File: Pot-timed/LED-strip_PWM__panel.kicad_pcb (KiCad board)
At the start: 2 copper layers, 160 x 100 mm, 549 parts, among them IC1 ATTINY13A-MM, P1 CONN_2, P2 CONN_2, T1 AO3400, U1 MCP1804-SOT23-5

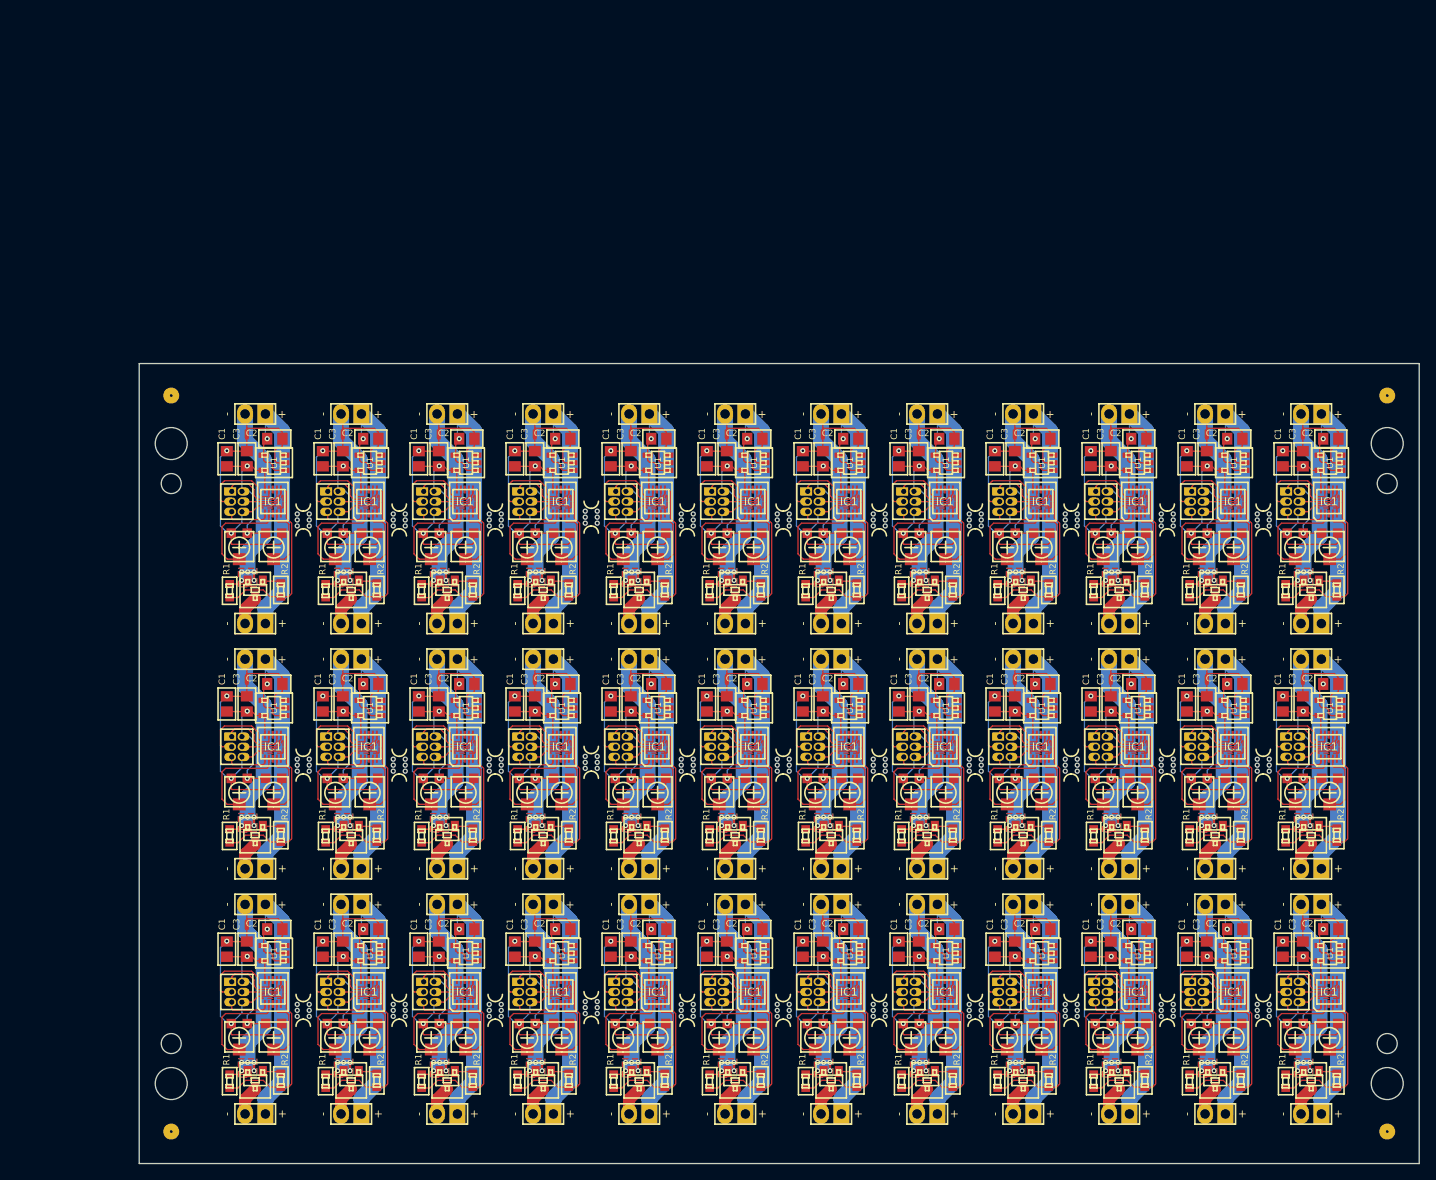
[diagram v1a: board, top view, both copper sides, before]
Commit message: Pot-timed: Reworking the panel.
KiCad really ought to know about the concept of 'linked clones' for boards.
Modify the 'parent' and all clones get updated automatically.
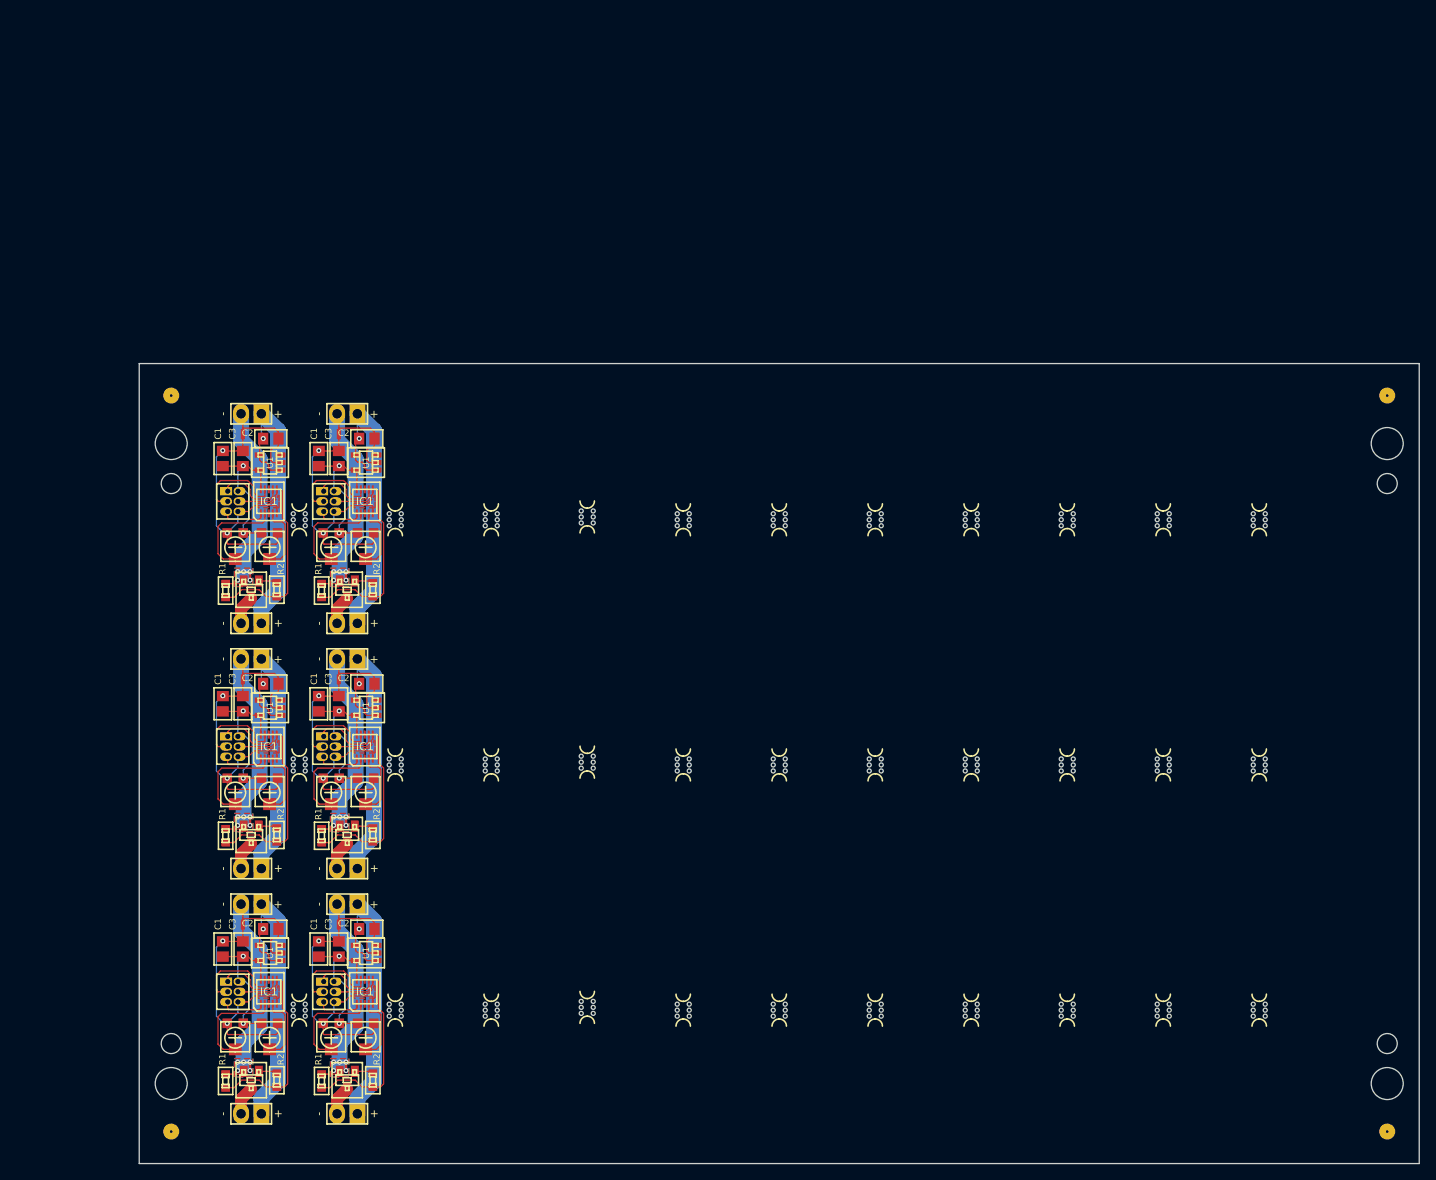
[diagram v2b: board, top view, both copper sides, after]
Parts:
- removed the C1 at (111.0, 93.9)
- removed the C1 at (218.9, 93.9)
- removed the C1 at (230.9, 93.9)
- removed the C1 at (242.9, 93.9)
- removed the C1 at (242.9, 124.5)
- removed the C1 at (230.9, 124.5)
- removed the C1 at (218.9, 124.5)
- removed the C1 at (182.9, 124.5)
- removed the C1 at (194.9, 124.5)
- removed the C1 at (206.9, 124.5)
- removed the C1 at (170.9, 124.5)
- removed the C1 at (146.9, 93.9)
- removed the C1 at (158.9, 124.5)
- removed the C1 at (123.0, 124.5)
- removed the C1 at (134.9, 124.5)
- removed the C1 at (146.9, 124.5)
- removed the C1 at (111.0, 124.5)
- removed the C1 at (111.0, 155.2)
- removed the C1 at (146.9, 155.2)
- removed the C1 at (134.9, 155.2)
- removed the C1 at (123.0, 155.2)
- removed the C1 at (158.9, 155.2)
- removed the C1 at (134.9, 93.9)
- removed the C1 at (170.9, 155.2)
- removed the C1 at (206.9, 155.2)
- removed the C1 at (194.9, 155.2)
- removed the C1 at (182.9, 155.2)
- removed the C1 at (218.9, 155.2)
- removed the C1 at (230.9, 155.2)
- removed the C1 at (242.9, 155.2)
- removed the C1 at (123.0, 93.9)
- removed the C1 at (158.9, 93.9)
- removed the C1 at (170.9, 93.9)
- removed the C1 at (206.9, 93.9)
- removed the C1 at (194.9, 93.9)
- removed the C1 at (182.9, 93.9)
- removed the C2 at (117.0, 91.4)
- removed the C2 at (224.9, 91.4)
- removed the C2 at (236.9, 91.4)
- removed the C2 at (248.9, 91.4)
- removed the C2 at (248.9, 122.0)
- removed the C2 at (236.9, 122.0)
- removed the C2 at (224.9, 122.0)
- removed the C2 at (188.9, 122.0)
- removed the C2 at (200.9, 122.0)
- removed the C2 at (212.9, 122.0)
- removed the C2 at (176.9, 122.0)
- removed the C2 at (152.9, 91.4)
- removed the C2 at (164.9, 122.0)
- removed the C2 at (128.9, 122.0)
- removed the C2 at (140.9, 122.0)
- removed the C2 at (152.9, 122.0)
- removed the C2 at (117.0, 122.0)
- removed the C2 at (117.0, 152.7)
- removed the C2 at (152.9, 152.7)
- removed the C2 at (140.9, 152.7)
- removed the C2 at (128.9, 152.7)
- removed the C2 at (164.9, 152.7)
- removed the C2 at (140.9, 91.4)
- removed the C2 at (176.9, 152.7)
- removed the C2 at (212.9, 152.7)
- removed the C2 at (200.9, 152.7)
- removed the C2 at (188.9, 152.7)
- removed the C2 at (224.9, 152.7)
- removed the C2 at (236.9, 152.7)
- removed the C2 at (248.9, 152.7)
- removed the C2 at (128.9, 91.4)
- removed the C2 at (164.9, 91.4)
- removed the C2 at (176.9, 91.4)
- removed the C2 at (212.9, 91.4)
- removed the C2 at (200.9, 91.4)
- removed the C2 at (188.9, 91.4)
- removed the C3 at (113.5, 93.9)
- removed the C3 at (221.4, 93.9)
- removed the C3 at (233.4, 93.9)
- removed the C3 at (245.4, 93.9)
- removed the C3 at (245.4, 124.5)
- removed the C3 at (233.4, 124.5)
- removed the C3 at (221.4, 124.5)
- removed the C3 at (185.4, 124.5)
- removed the C3 at (197.4, 124.5)
- removed the C3 at (209.4, 124.5)
- removed the C3 at (173.4, 124.5)
- removed the C3 at (149.4, 93.9)
- removed the C3 at (161.4, 124.5)
- removed the C3 at (125.5, 124.5)
- removed the C3 at (137.4, 124.5)
- removed the C3 at (149.4, 124.5)
- removed the C3 at (113.5, 124.5)
- removed the C3 at (113.5, 155.2)
- removed the C3 at (149.4, 155.2)
- removed the C3 at (137.4, 155.2)
- removed the C3 at (125.5, 155.2)
- removed the C3 at (161.4, 155.2)
- removed the C3 at (137.4, 93.9)
- removed the C3 at (173.4, 155.2)
- removed the C3 at (209.4, 155.2)
- removed the C3 at (197.4, 155.2)
- removed the C3 at (185.4, 155.2)
- removed the C3 at (221.4, 155.2)
- removed the C3 at (233.4, 155.2)
- removed the C3 at (245.4, 155.2)
- removed the C3 at (125.5, 93.9)
- removed the C3 at (161.4, 93.9)
- removed the C3 at (173.4, 93.9)
- removed the C3 at (209.4, 93.9)
- removed the C3 at (197.4, 93.9)
- removed the C3 at (185.4, 93.9)
- removed the IC1 at (116.7, 99.2)
- removed the IC1 at (224.7, 99.2)
- removed the IC1 at (236.7, 99.2)
- removed the IC1 at (248.7, 99.2)
- removed the IC1 at (248.7, 129.9)
- removed the IC1 at (236.7, 129.9)
- removed the IC1 at (224.7, 129.9)
- removed the IC1 at (188.7, 129.9)
- removed the IC1 at (200.7, 129.9)
- removed the IC1 at (212.7, 129.9)
- removed the IC1 at (176.7, 129.9)
- removed the IC1 at (152.7, 99.2)
- removed the IC1 at (164.7, 129.9)
- removed the IC1 at (128.7, 129.9)
- removed the IC1 at (140.7, 129.9)
- removed the IC1 at (152.7, 129.9)
- removed the IC1 at (116.7, 129.9)
- removed the IC1 at (116.7, 160.6)
- removed the IC1 at (152.7, 160.6)
- removed the IC1 at (140.7, 160.6)
- removed the IC1 at (128.7, 160.6)
- removed the IC1 at (164.7, 160.6)
- removed the IC1 at (140.7, 99.2)
- removed the IC1 at (176.7, 160.6)
- removed the IC1 at (212.7, 160.6)
- removed the IC1 at (200.7, 160.6)
- removed the IC1 at (188.7, 160.6)
- removed the IC1 at (224.7, 160.6)
- removed the IC1 at (236.7, 160.6)
- removed the IC1 at (248.7, 160.6)
- removed the IC1 at (128.7, 99.2)
- removed the IC1 at (164.7, 99.2)
- removed the IC1 at (176.7, 99.2)
- removed the IC1 at (212.7, 99.2)
- removed the IC1 at (200.7, 99.2)
- removed the IC1 at (188.7, 99.2)
- removed the JP1 at (112.2, 99.2)
- removed the JP1 at (220.2, 99.2)
- removed the JP1 at (232.2, 99.2)
- removed the JP1 at (244.2, 99.2)
- removed the JP1 at (244.2, 129.9)
- removed the JP1 at (232.2, 129.9)
- removed the JP1 at (220.2, 129.9)
- removed the JP1 at (184.2, 129.9)
- removed the JP1 at (196.2, 129.9)
- removed the JP1 at (208.2, 129.9)
- removed the JP1 at (172.2, 129.9)
- removed the JP1 at (148.2, 99.2)
- removed the JP1 at (160.2, 129.9)
- removed the JP1 at (124.2, 129.9)
- removed the JP1 at (136.2, 129.9)
- removed the JP1 at (148.2, 129.9)
- removed the JP1 at (112.2, 129.9)
- removed the JP1 at (112.2, 160.6)
- removed the JP1 at (148.2, 160.6)
- removed the JP1 at (136.2, 160.6)
- removed the JP1 at (124.2, 160.6)
- removed the JP1 at (160.2, 160.6)
- removed the JP1 at (136.2, 99.2)
- removed the JP1 at (172.2, 160.6)
- removed the JP1 at (208.2, 160.6)
- removed the JP1 at (196.2, 160.6)
- removed the JP1 at (184.2, 160.6)
- removed the JP1 at (220.2, 160.6)
- removed the JP1 at (232.2, 160.6)
- removed the JP1 at (244.2, 160.6)
- removed the JP1 at (124.2, 99.2)
- removed the JP1 at (160.2, 99.2)
- removed the JP1 at (172.2, 99.2)
- removed the JP1 at (208.2, 99.2)
- removed the JP1 at (196.2, 99.2)
- removed the JP1 at (184.2, 99.2)
- removed the NJ1 at (113.5, 90.8)
- removed the NJ1 at (221.4, 90.8)
- removed the NJ1 at (233.4, 90.8)
- removed the NJ1 at (245.4, 90.8)
- removed the NJ1 at (245.4, 121.5)
- removed the NJ1 at (233.4, 121.5)
- removed the NJ1 at (221.4, 121.5)
- removed the NJ1 at (185.4, 121.5)
- removed the NJ1 at (197.4, 121.5)
- removed the NJ1 at (209.4, 121.5)
- removed the NJ1 at (173.4, 121.5)
- removed the NJ1 at (149.4, 90.8)
- removed the NJ1 at (161.4, 121.5)
- removed the NJ1 at (125.5, 121.5)
- removed the NJ1 at (137.4, 121.5)
- removed the NJ1 at (149.4, 121.5)
- removed the NJ1 at (113.5, 121.5)
- removed the NJ1 at (113.5, 152.2)
- removed the NJ1 at (149.4, 152.2)
- removed the NJ1 at (137.4, 152.2)
- removed the NJ1 at (125.5, 152.2)
- removed the NJ1 at (161.4, 152.2)
- removed the NJ1 at (137.4, 90.8)
- removed the NJ1 at (173.4, 152.2)
- removed the NJ1 at (209.4, 152.2)
- removed the NJ1 at (197.4, 152.2)
- removed the NJ1 at (185.4, 152.2)
- removed the NJ1 at (221.4, 152.2)
- removed the NJ1 at (233.4, 152.2)
- removed the NJ1 at (245.4, 152.2)
- removed the NJ1 at (125.5, 90.8)
- removed the NJ1 at (161.4, 90.8)
- removed the NJ1 at (173.4, 90.8)
- removed the NJ1 at (209.4, 90.8)
- removed the NJ1 at (197.4, 90.8)
- removed the NJ1 at (185.4, 90.8)
- removed the P1 at (114.5, 88.3)
- removed the P1 at (222.5, 88.3)
- removed the P1 at (234.5, 88.3)
- removed the P1 at (246.5, 88.3)
- removed the P1 at (246.5, 119.0)
- removed the P1 at (234.5, 119.0)
- removed the P1 at (222.5, 119.0)
- removed the P1 at (186.5, 119.0)
- removed the P1 at (198.5, 119.0)
- removed the P1 at (210.5, 119.0)
- removed the P1 at (174.5, 119.0)
- removed the P1 at (150.5, 88.3)
- removed the P1 at (162.5, 119.0)
- removed the P1 at (126.5, 119.0)
- removed the P1 at (138.5, 119.0)
- removed the P1 at (150.5, 119.0)
- removed the P1 at (114.5, 119.0)
- removed the P1 at (114.5, 149.6)
- removed the P1 at (150.5, 149.6)
- removed the P1 at (138.5, 149.6)
- removed the P1 at (126.5, 149.6)
- removed the P1 at (162.5, 149.6)
- removed the P1 at (138.5, 88.3)
- removed the P1 at (174.5, 149.6)
- removed the P1 at (210.5, 149.6)
- removed the P1 at (198.5, 149.6)
- removed the P1 at (186.5, 149.6)
- removed the P1 at (222.5, 149.6)
- removed the P1 at (234.5, 149.6)
- removed the P1 at (246.5, 149.6)
- removed the P1 at (126.5, 88.3)
- removed the P1 at (162.5, 88.3)
- removed the P1 at (174.5, 88.3)
- removed the P1 at (210.5, 88.3)
- removed the P1 at (198.5, 88.3)
- removed the P1 at (186.5, 88.3)
- removed the P2 at (114.5, 114.5)
- removed the P2 at (222.5, 114.5)
- removed the P2 at (234.5, 114.5)
- removed the P2 at (246.5, 114.5)
- removed the P2 at (246.5, 145.2)
- removed the P2 at (234.5, 145.2)
- removed the P2 at (222.5, 145.2)
- removed the P2 at (186.5, 145.2)
- removed the P2 at (198.5, 145.2)
- removed the P2 at (210.5, 145.2)
- removed the P2 at (174.5, 145.2)
- removed the P2 at (150.5, 114.5)
- removed the P2 at (162.5, 145.2)
- removed the P2 at (126.5, 145.2)
- removed the P2 at (138.5, 145.2)
- removed the P2 at (150.5, 145.2)
- removed the P2 at (114.5, 145.2)
- removed the P2 at (114.5, 175.8)
- removed the P2 at (150.5, 175.8)
- removed the P2 at (138.5, 175.8)
- removed the P2 at (126.5, 175.8)
- removed the P2 at (162.5, 175.8)
- removed the P2 at (138.5, 114.5)
- removed the P2 at (174.5, 175.8)
- removed the P2 at (210.5, 175.8)
- removed the P2 at (198.5, 175.8)
- removed the P2 at (186.5, 175.8)
- removed the P2 at (222.5, 175.8)
- removed the P2 at (234.5, 175.8)
- removed the P2 at (246.5, 175.8)
- removed the P2 at (126.5, 114.5)
- removed the P2 at (162.5, 114.5)
- removed the P2 at (174.5, 114.5)
- removed the P2 at (210.5, 114.5)
- removed the P2 at (198.5, 114.5)
- removed the P2 at (186.5, 114.5)
- removed the R1 at (111.3, 110.4)
- removed the R1 at (219.3, 110.4)
- removed the R1 at (231.3, 110.4)
- removed the R1 at (243.3, 110.4)
- removed the R1 at (243.3, 141.1)
- removed the R1 at (231.3, 141.1)
- removed the R1 at (219.3, 141.1)
- removed the R1 at (183.3, 141.1)
- removed the R1 at (195.3, 141.1)
- removed the R1 at (207.3, 141.1)
- removed the R1 at (171.3, 141.1)
- removed the R1 at (147.3, 110.4)
- removed the R1 at (159.3, 141.1)
- removed the R1 at (123.3, 141.1)
- removed the R1 at (135.3, 141.1)
- removed the R1 at (147.3, 141.1)
- removed the R1 at (111.3, 141.1)
- removed the R1 at (111.3, 171.7)
- removed the R1 at (147.3, 171.7)
- removed the R1 at (135.3, 171.7)
- removed the R1 at (123.3, 171.7)
- removed the R1 at (159.3, 171.7)
- removed the R1 at (135.3, 110.4)
- removed the R1 at (171.3, 171.7)
- removed the R1 at (207.3, 171.7)
- removed the R1 at (195.3, 171.7)
- removed the R1 at (183.3, 171.7)
- removed the R1 at (219.3, 171.7)
- removed the R1 at (231.3, 171.7)
- removed the R1 at (243.3, 171.7)
- removed the R1 at (123.3, 110.4)
- removed the R1 at (159.3, 110.4)
- removed the R1 at (171.3, 110.4)
- removed the R1 at (207.3, 110.4)
- removed the R1 at (195.3, 110.4)
- removed the R1 at (183.3, 110.4)
- removed the R2 at (117.7, 110.3)
- removed the R2 at (225.7, 110.3)
- removed the R2 at (237.7, 110.3)
- removed the R2 at (249.7, 110.3)
- removed the R2 at (249.7, 140.9)
- removed the R2 at (237.7, 140.9)
- removed the R2 at (225.7, 140.9)
- removed the R2 at (189.7, 140.9)
- removed the R2 at (201.7, 140.9)
- removed the R2 at (213.7, 140.9)
- removed the R2 at (177.7, 140.9)
- removed the R2 at (153.7, 110.3)
- removed the R2 at (165.7, 140.9)
- removed the R2 at (129.7, 140.9)
- removed the R2 at (141.7, 140.9)
- removed the R2 at (153.7, 140.9)
- removed the R2 at (117.7, 140.9)
- removed the R2 at (117.7, 171.6)
- removed the R2 at (153.7, 171.6)
- removed the R2 at (141.7, 171.6)
- removed the R2 at (129.7, 171.6)
- removed the R2 at (165.7, 171.6)
- removed the R2 at (141.7, 110.3)
- removed the R2 at (177.7, 171.6)
- removed the R2 at (213.7, 171.6)
- removed the R2 at (201.7, 171.6)
- removed the R2 at (189.7, 171.6)
- removed the R2 at (225.7, 171.6)
- removed the R2 at (237.7, 171.6)
- removed the R2 at (249.7, 171.6)
- removed the R2 at (129.7, 110.3)
- removed the R2 at (165.7, 110.3)
- removed the R2 at (177.7, 110.3)
- removed the R2 at (213.7, 110.3)
- removed the R2 at (201.7, 110.3)
- removed the R2 at (189.7, 110.3)
- removed the RV1 at (112.5, 105.0)
- removed the RV1 at (220.5, 105.0)
- removed the RV1 at (232.5, 105.0)
- removed the RV1 at (244.5, 105.0)
- removed the RV1 at (244.5, 135.7)
- removed the RV1 at (232.5, 135.7)
- removed the RV1 at (220.5, 135.7)
- removed the RV1 at (184.5, 135.7)
- removed the RV1 at (196.5, 135.7)
- removed the RV1 at (208.5, 135.7)
- removed the RV1 at (172.5, 135.7)
- removed the RV1 at (148.5, 105.0)
- removed the RV1 at (160.5, 135.7)
- removed the RV1 at (124.5, 135.7)
- removed the RV1 at (136.5, 135.7)
- removed the RV1 at (148.5, 135.7)
- removed the RV1 at (112.5, 135.7)
- removed the RV1 at (112.5, 166.3)
- removed the RV1 at (148.5, 166.3)
- removed the RV1 at (136.5, 166.3)
- removed the RV1 at (124.5, 166.3)
- removed the RV1 at (160.5, 166.3)
- removed the RV1 at (136.5, 105.0)
- removed the RV1 at (172.5, 166.3)
- removed the RV1 at (208.5, 166.3)
- removed the RV1 at (196.5, 166.3)
- removed the RV1 at (184.5, 166.3)
- removed the RV1 at (220.5, 166.3)
- removed the RV1 at (232.5, 166.3)
- removed the RV1 at (244.5, 166.3)
- removed the RV1 at (124.5, 105.0)
- removed the RV1 at (160.5, 105.0)
- removed the RV1 at (172.5, 105.0)
- removed the RV1 at (208.5, 105.0)
- removed the RV1 at (196.5, 105.0)
- removed the RV1 at (184.5, 105.0)
- removed the RV2 at (116.8, 105.0)
- removed the RV2 at (224.8, 105.0)
- removed the RV2 at (236.8, 105.0)
- removed the RV2 at (248.8, 105.0)
- removed the RV2 at (248.8, 135.7)
- removed the RV2 at (236.8, 135.7)
- removed the RV2 at (224.8, 135.7)
- removed the RV2 at (188.8, 135.7)
- removed the RV2 at (200.8, 135.7)
- removed the RV2 at (212.8, 135.7)
- removed the RV2 at (176.8, 135.7)
- removed the RV2 at (152.8, 105.0)
- removed the RV2 at (164.8, 135.7)
- removed the RV2 at (128.8, 135.7)
- removed the RV2 at (140.8, 135.7)
- removed the RV2 at (152.8, 135.7)
- removed the RV2 at (116.8, 135.7)
- removed the RV2 at (116.8, 166.3)
- removed the RV2 at (152.8, 166.3)
- removed the RV2 at (140.8, 166.3)
- removed the RV2 at (128.8, 166.3)
- removed the RV2 at (164.8, 166.3)
- removed the RV2 at (140.8, 105.0)
- removed the RV2 at (176.8, 166.3)
- removed the RV2 at (212.8, 166.3)
- removed the RV2 at (200.8, 166.3)
- removed the RV2 at (188.8, 166.3)
- removed the RV2 at (224.8, 166.3)
- removed the RV2 at (236.8, 166.3)
- removed the RV2 at (248.8, 166.3)
- removed the RV2 at (128.8, 105.0)
- removed the RV2 at (164.8, 105.0)
- removed the RV2 at (176.8, 105.0)
- removed the RV2 at (212.8, 105.0)
- removed the RV2 at (200.8, 105.0)
- removed the RV2 at (188.8, 105.0)
- removed the T1 at (114.5, 110.3)
- removed the T1 at (222.5, 110.3)
- removed the T1 at (234.5, 110.3)
- removed the T1 at (246.5, 110.3)
- removed the T1 at (246.5, 140.9)
- removed the T1 at (234.5, 140.9)
- removed the T1 at (222.5, 140.9)
- removed the T1 at (186.5, 140.9)
- removed the T1 at (198.5, 140.9)
- removed the T1 at (210.5, 140.9)
- removed the T1 at (174.5, 140.9)
- removed the T1 at (150.5, 110.3)
- removed the T1 at (162.5, 140.9)
- removed the T1 at (126.5, 140.9)
- removed the T1 at (138.5, 140.9)
- removed the T1 at (150.5, 140.9)
- removed the T1 at (114.5, 140.9)
- removed the T1 at (114.5, 171.6)
- removed the T1 at (150.5, 171.6)
- removed the T1 at (138.5, 171.6)
- removed the T1 at (126.5, 171.6)
- removed the T1 at (162.5, 171.6)
- removed the T1 at (138.5, 110.3)
- removed the T1 at (174.5, 171.6)
- removed the T1 at (210.5, 171.6)
- removed the T1 at (198.5, 171.6)
- removed the T1 at (186.5, 171.6)
- removed the T1 at (222.5, 171.6)
- removed the T1 at (234.5, 171.6)
- removed the T1 at (246.5, 171.6)
- removed the T1 at (126.5, 110.3)
- removed the T1 at (162.5, 110.3)
- removed the T1 at (174.5, 110.3)
- removed the T1 at (210.5, 110.3)
- removed the T1 at (198.5, 110.3)
- removed the T1 at (186.5, 110.3)
- removed the U1 at (116.8, 94.4)
- removed the U1 at (224.8, 94.4)
- removed the U1 at (236.8, 94.4)
- removed the U1 at (248.8, 94.4)
- removed the U1 at (248.8, 125.0)
- removed the U1 at (236.8, 125.0)
- removed the U1 at (224.8, 125.0)
- removed the U1 at (188.8, 125.0)
- removed the U1 at (200.8, 125.0)
- removed the U1 at (212.8, 125.0)
- removed the U1 at (176.8, 125.0)
- removed the U1 at (152.8, 94.4)
- removed the U1 at (164.8, 125.0)
- removed the U1 at (128.8, 125.0)
- removed the U1 at (140.8, 125.0)
- removed the U1 at (152.8, 125.0)
- removed the U1 at (116.8, 125.0)
- removed the U1 at (116.8, 155.7)
- removed the U1 at (152.8, 155.7)
- removed the U1 at (140.8, 155.7)
- removed the U1 at (128.8, 155.7)
- removed the U1 at (164.8, 155.7)
- removed the U1 at (140.8, 94.4)
- removed the U1 at (176.8, 155.7)
- removed the U1 at (212.8, 155.7)
- removed the U1 at (200.8, 155.7)
- removed the U1 at (188.8, 155.7)
- removed the U1 at (224.8, 155.7)
- removed the U1 at (236.8, 155.7)
- removed the U1 at (248.8, 155.7)
- removed the U1 at (128.8, 94.4)
- removed the U1 at (164.8, 94.4)
- removed the U1 at (176.8, 94.4)
- removed the U1 at (212.8, 94.4)
- removed the U1 at (200.8, 94.4)
- removed the U1 at (188.8, 94.4)
- added C1: 100nF, MADW__C0805, F.Cu at (122.5, 93.9)
- added C1: 100nF, MADW__C0805, F.Cu at (122.5, 124.5)
- added C1: 100nF, MADW__C0805, F.Cu at (122.5, 155.2)
- added C1: 100nF, MADW__C0805, F.Cu at (110.5, 155.2)
- added C1: 100nF, MADW__C0805, F.Cu at (110.5, 124.5)
- added C1: 100nF, MADW__C0805, F.Cu at (110.5, 93.9)
- added C2: 100nF, MADW__C0805, F.Cu at (128.4, 91.4)
- added C2: 100nF, MADW__C0805, F.Cu at (128.4, 122.0)
- added C2: 100nF, MADW__C0805, F.Cu at (128.4, 152.7)
- added C2: 100nF, MADW__C0805, F.Cu at (116.5, 152.7)
- added C2: 100nF, MADW__C0805, F.Cu at (116.5, 122.0)
- added C2: 100nF, MADW__C0805, F.Cu at (116.5, 91.4)
- added C3: 4.7µF, MADW__C0805, F.Cu at (125.0, 93.9)
- added C3: 4.7µF, MADW__C0805, F.Cu at (125.0, 124.5)
- added C3: 4.7µF, MADW__C0805, F.Cu at (125.0, 155.2)
- added C3: 4.7µF, MADW__C0805, F.Cu at (113.0, 155.2)
- added C3: 4.7µF, MADW__C0805, F.Cu at (113.0, 124.5)
- added C3: 4.7µF, MADW__C0805, F.Cu at (113.0, 93.9)
- added IC1: ATTINY13A-MM, MADW__MLF10, F.Cu at (128.2, 99.2)
- added IC1: ATTINY13A-MM, MADW__MLF10, F.Cu at (128.2, 129.9)
- added IC1: ATTINY13A-MM, MADW__MLF10, F.Cu at (128.2, 160.5)
- added IC1: ATTINY13A-MM, MADW__MLF10, F.Cu at (116.2, 160.5)
- added IC1: ATTINY13A-MM, MADW__MLF10, F.Cu at (116.2, 129.9)
- added IC1: ATTINY13A-MM, MADW__MLF10, F.Cu at (116.2, 99.2)
- added JP1: ISP, MADW__PIN_ARRAY_3x2_1.27mm, F.Cu at (123.7, 99.2)
- added JP1: ISP, MADW__PIN_ARRAY_3x2_1.27mm, F.Cu at (123.7, 129.9)
- added JP1: ISP, MADW__PIN_ARRAY_3x2_1.27mm, F.Cu at (123.7, 160.5)
- added JP1: ISP, MADW__PIN_ARRAY_3x2_1.27mm, F.Cu at (111.7, 160.5)
- added JP1: ISP, MADW__PIN_ARRAY_3x2_1.27mm, F.Cu at (111.7, 129.9)
- added JP1: ISP, MADW__PIN_ARRAY_3x2_1.27mm, F.Cu at (111.7, 99.2)
- added NJ1: NET-JOIN, MADW__SMD-net-noin-0.5mm, F.Cu at (125.0, 90.8)
- added NJ1: NET-JOIN, MADW__SMD-net-noin-0.5mm, F.Cu at (125.0, 121.5)
- added NJ1: NET-JOIN, MADW__SMD-net-noin-0.5mm, F.Cu at (125.0, 152.1)
- added NJ1: NET-JOIN, MADW__SMD-net-noin-0.5mm, F.Cu at (113.0, 152.1)
- added NJ1: NET-JOIN, MADW__SMD-net-noin-0.5mm, F.Cu at (113.0, 121.5)
- added NJ1: NET-JOIN, MADW__SMD-net-noin-0.5mm, F.Cu at (113.0, 90.8)
- added P1: CONN_2, MADW__SIL-2, F.Cu at (126.0, 88.3)
- added P1: CONN_2, MADW__SIL-2, F.Cu at (126.0, 118.9)
- added P1: CONN_2, MADW__SIL-2, F.Cu at (126.0, 149.6)
- added P1: CONN_2, MADW__SIL-2, F.Cu at (114.0, 149.6)
- added P1: CONN_2, MADW__SIL-2, F.Cu at (114.0, 118.9)
- added P1: CONN_2, MADW__SIL-2, F.Cu at (114.0, 88.3)
- added P2: CONN_2, MADW__SIL-2, F.Cu at (126.0, 114.5)
- added P2: CONN_2, MADW__SIL-2, F.Cu at (126.0, 145.1)
- added P2: CONN_2, MADW__SIL-2, F.Cu at (126.0, 175.8)
- added P2: CONN_2, MADW__SIL-2, F.Cu at (114.0, 175.8)
- added P2: CONN_2, MADW__SIL-2, F.Cu at (114.0, 145.1)
- added P2: CONN_2, MADW__SIL-2, F.Cu at (114.0, 114.5)
- added R1: 100k, MADW__R0603_2, F.Cu at (122.8, 110.4)
- added R1: 100k, MADW__R0603_2, F.Cu at (122.8, 141.0)
- added R1: 100k, MADW__R0603_2, F.Cu at (122.8, 171.7)
- added R1: 100k, MADW__R0603_2, F.Cu at (110.8, 171.7)
- added R1: 100k, MADW__R0603_2, F.Cu at (110.8, 141.0)
- added R1: 100k, MADW__R0603_2, F.Cu at (110.8, 110.4)
- added R2: 150R, MADW__R0603_2, F.Cu at (129.2, 110.3)
- added R2: 150R, MADW__R0603_2, F.Cu at (129.2, 140.9)
- added R2: 150R, MADW__R0603_2, F.Cu at (129.2, 171.6)
- added R2: 150R, MADW__R0603_2, F.Cu at (117.2, 171.6)
- added R2: 150R, MADW__R0603_2, F.Cu at (117.2, 140.9)
- added R2: 150R, MADW__R0603_2, F.Cu at (117.2, 110.3)
- added RV1: 50k, MADW__TC33X-POT, F.Cu at (124.0, 105.0)
- added RV1: 50k, MADW__TC33X-POT, F.Cu at (124.0, 135.6)
- added RV1: 50k, MADW__TC33X-POT, F.Cu at (124.0, 166.3)
- added RV1: 50k, MADW__TC33X-POT, F.Cu at (112.0, 166.3)
- added RV1: 50k, MADW__TC33X-POT, F.Cu at (112.0, 135.6)
- added RV1: 50k, MADW__TC33X-POT, F.Cu at (112.0, 105.0)
- added RV2: 50k, MADW__TC33X-POT, F.Cu at (128.3, 105.0)
- added RV2: 50k, MADW__TC33X-POT, F.Cu at (128.3, 135.6)
- added RV2: 50k, MADW__TC33X-POT, F.Cu at (128.3, 166.3)
- added RV2: 50k, MADW__TC33X-POT, F.Cu at (116.3, 166.3)
- added RV2: 50k, MADW__TC33X-POT, F.Cu at (116.3, 135.6)
- added RV2: 50k, MADW__TC33X-POT, F.Cu at (116.3, 105.0)
- added T1: AO3400, MADW__SOT23, F.Cu at (126.0, 110.3)
- added T1: AO3400, MADW__SOT23, F.Cu at (126.0, 140.9)
- added T1: AO3400, MADW__SOT23, F.Cu at (126.0, 171.6)
- added T1: AO3400, MADW__SOT23, F.Cu at (114.0, 171.6)
- added T1: AO3400, MADW__SOT23, F.Cu at (114.0, 140.9)
- added T1: AO3400, MADW__SOT23, F.Cu at (114.0, 110.3)
- added U1: MCP1804-SOT23-5, MADW__SOT23-5, F.Cu at (128.3, 94.4)
- added U1: MCP1804-SOT23-5, MADW__SOT23-5, F.Cu at (128.3, 125.0)
- added U1: MCP1804-SOT23-5, MADW__SOT23-5, F.Cu at (128.3, 155.7)
- added U1: MCP1804-SOT23-5, MADW__SOT23-5, F.Cu at (116.3, 155.7)
- added U1: MCP1804-SOT23-5, MADW__SOT23-5, F.Cu at (116.3, 125.0)
- added U1: MCP1804-SOT23-5, MADW__SOT23-5, F.Cu at (116.3, 94.4)
- moved mouse-bite-2mm 0.50 mm to (156.0, 131.8)
- moved mouse-bite-2mm 0.50 mm to (156.0, 162.5)
- moved mouse-bite-2mm 0.50 mm to (132.0, 162.8)
- moved mouse-bite-2mm 0.50 mm to (144.0, 162.8)
- moved mouse-bite-2mm 0.50 mm to (180.0, 162.8)
- moved mouse-bite-2mm 0.50 mm to (168.0, 162.8)
- moved mouse-bite-2mm 0.50 mm to (192.0, 162.8)
- moved mouse-bite-2mm 0.50 mm to (204.0, 162.8)
- moved mouse-bite-2mm 0.50 mm to (240.0, 162.8)
- moved mouse-bite-2mm 0.50 mm to (228.0, 162.8)
- moved mouse-bite-2mm 0.50 mm to (216.0, 162.8)
- moved mouse-bite-2mm 0.50 mm to (120.0, 162.8)
- moved mouse-bite-2mm 0.50 mm to (156.0, 101.2)
- moved mouse-bite-2mm 0.50 mm to (180.0, 101.5)
- moved mouse-bite-2mm 0.50 mm to (144.0, 101.5)
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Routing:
- net GNDPWR: track 1478.7 -> 246.5 mm, vias 180 -> 30
- net /Vin: track 1344.7 -> 224.1 mm, vias 36 -> 6
- net GND: track 1229.0 -> 204.8 mm, vias 72 -> 12
- net /MOSI: track 1050.6 -> 175.1 mm
- net VCC: track 719.0 -> 119.8 mm, vias 72 -> 12
- net /POT1: track 464.7 -> 77.5 mm
- net /SCK: track 424.1 -> 70.7 mm
- net /MISO: track 311.8 -> 52.0 mm
- net /POT2: track 306.5 -> 51.1 mm
- net /RESET: track 204.1 -> 34.0 mm
- net /drain: track 130.5 -> 21.8 mm
- net N-000004: track 99.2 -> 16.5 mm

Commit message: Pot-timed: Forgot logos. Panel now 100% V-groove.
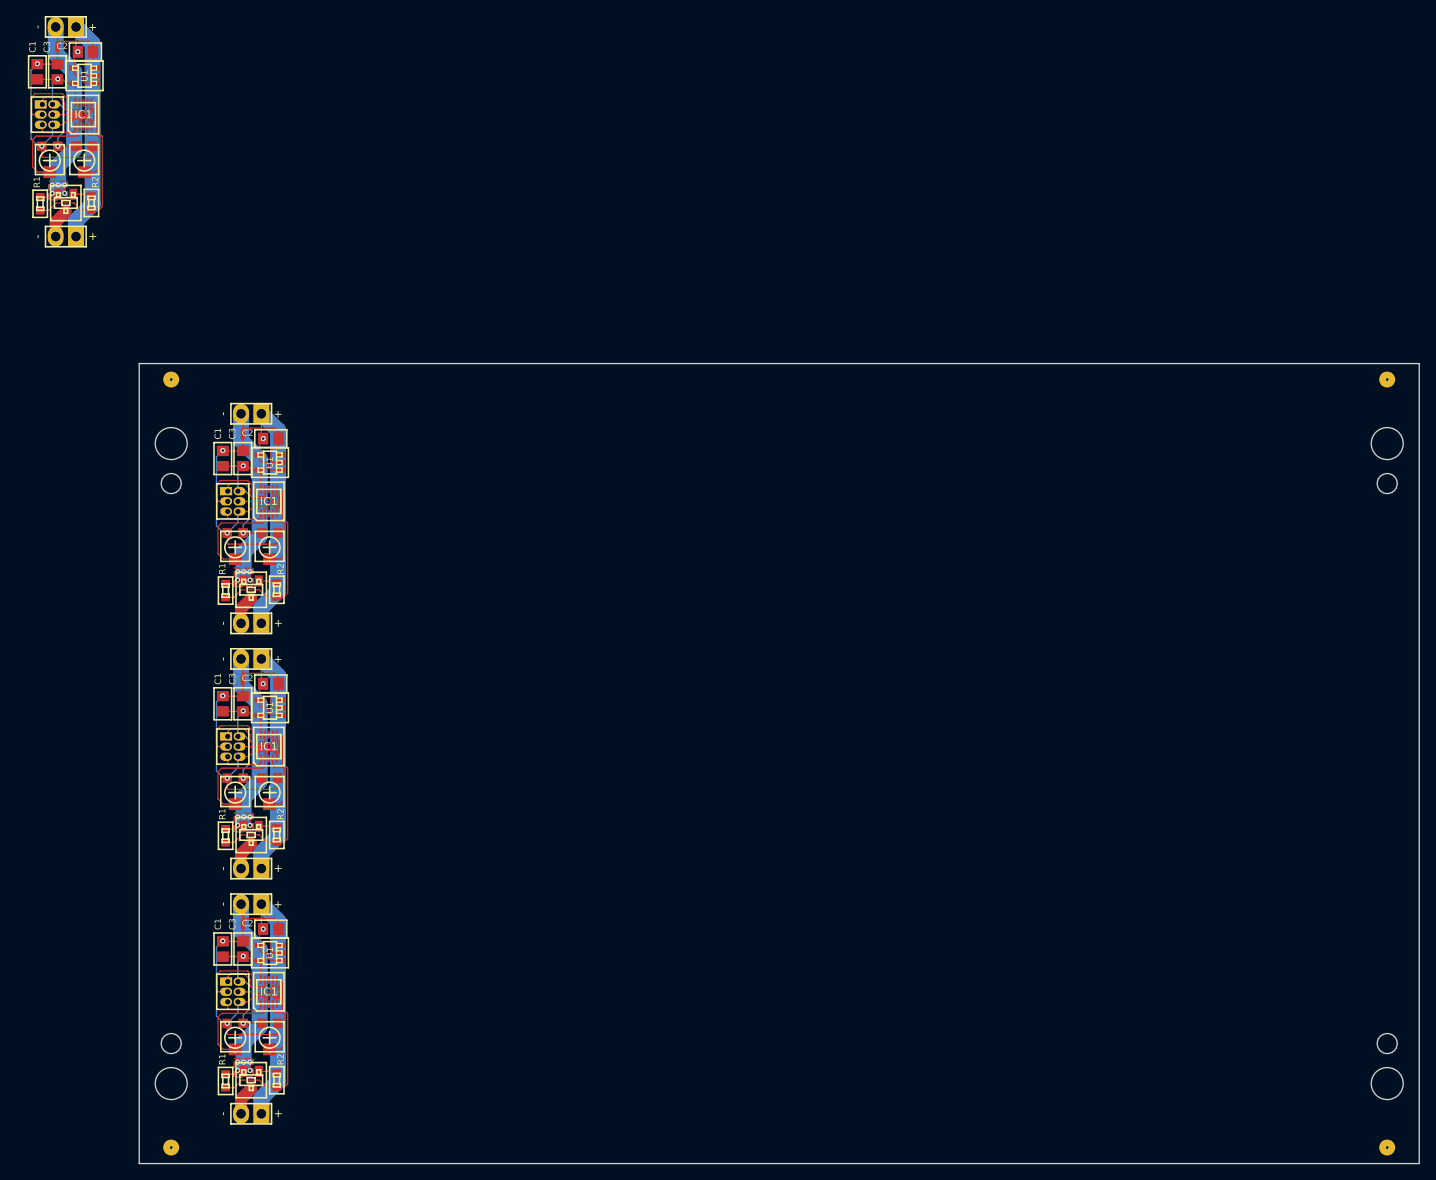
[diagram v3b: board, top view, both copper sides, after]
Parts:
- removed the C1 at (122.5, 93.9)
- removed the C1 at (122.5, 124.5)
- removed the C1 at (122.5, 155.2)
- removed the C2 at (128.4, 91.4)
- removed the C2 at (128.4, 122.0)
- removed the C2 at (128.4, 152.7)
- removed the C3 at (125.0, 93.9)
- removed the C3 at (125.0, 124.5)
- removed the C3 at (125.0, 155.2)
- removed the IC1 at (128.2, 99.2)
- removed the IC1 at (128.2, 129.9)
- removed the IC1 at (128.2, 160.5)
- removed the JP1 at (123.7, 99.2)
- removed the JP1 at (123.7, 129.9)
- removed the JP1 at (123.7, 160.5)
- removed the NJ1 at (125.0, 90.8)
- removed the NJ1 at (125.0, 121.5)
- removed the NJ1 at (125.0, 152.1)
- removed the P1 at (126.0, 88.3)
- removed the P1 at (126.0, 118.9)
- removed the P1 at (126.0, 149.6)
- removed the P2 at (126.0, 114.5)
- removed the P2 at (126.0, 145.1)
- removed the P2 at (126.0, 175.8)
- removed the R1 at (122.8, 110.4)
- removed the R1 at (122.8, 141.0)
- removed the R1 at (122.8, 171.7)
- removed the R2 at (129.2, 110.3)
- removed the R2 at (129.2, 140.9)
- removed the R2 at (129.2, 171.6)
- removed the RV1 at (124.0, 105.0)
- removed the RV1 at (124.0, 135.6)
- removed the RV1 at (124.0, 166.3)
- removed the RV2 at (128.3, 105.0)
- removed the RV2 at (128.3, 135.6)
- removed the RV2 at (128.3, 166.3)
- removed the T1 at (126.0, 110.3)
- removed the T1 at (126.0, 140.9)
- removed the T1 at (126.0, 171.6)
- removed the U1 at (128.3, 94.4)
- removed the U1 at (128.3, 125.0)
- removed the U1 at (128.3, 155.7)
- removed mouse-bite-2mm (x33): VAL**, MADW__mouse-bite-2mm-slot
- added C1: 100nF, MADW__C0805, F.Cu at (110.5, 93.9)
- added C2: 100nF, MADW__C0805, F.Cu at (116.5, 91.4)
- added C3: 4.7µF, MADW__C0805, F.Cu at (113.0, 93.9)
- added G1: OSHW-logo_silkscreen_3mm, OSHW-logo_silkscreen_3mm, B.Cu at (113.2, 166.8)
- added G1: OSHW-logo_silkscreen_3mm, OSHW-logo_silkscreen_3mm, B.Cu at (113.2, 136.1)
- added G1: OSHW-logo_silkscreen_3mm, OSHW-logo_silkscreen_3mm, B.Cu at (113.2, 105.5)
- added G1: OSHW-logo_silkscreen_3mm, OSHW-logo_silkscreen_3mm, B.Cu at (90.0, 57.1)
- added G2: LED_smile_silkscreen_3mm, LED_smile_silkscreen_3mm, B.Cu at (113.2, 154.7)
- added G2: LED_smile_silkscreen_3mm, LED_smile_silkscreen_3mm, B.Cu at (113.2, 124.1)
- added G2: LED_smile_silkscreen_3mm, LED_smile_silkscreen_3mm, B.Cu at (113.2, 93.4)
- added G2: LED_smile_silkscreen_3mm, LED_smile_silkscreen_3mm, B.Cu at (90.0, 45.1)
- added IC1: ATTINY13A-MM, MADW__MLF10, F.Cu at (116.2, 99.2)
- added JP1: ISP, MADW__PIN_ARRAY_3x2_1.27mm, F.Cu at (111.7, 99.2)
- added NJ1: NET-JOIN, MADW__SMD-net-noin-0.5mm, F.Cu at (113.0, 90.8)
- added P1: CONN_2, MADW__SIL-2, F.Cu at (114.0, 88.3)
- added P2: CONN_2, MADW__SIL-2, F.Cu at (114.0, 114.5)
- added R1: 100k, MADW__R0603_2, F.Cu at (110.8, 110.4)
- added R2: 150R, MADW__R0603_2, F.Cu at (117.2, 110.3)
- added RV1: 50k, MADW__TC33X-POT, F.Cu at (112.0, 105.0)
- added RV2: 50k, MADW__TC33X-POT, F.Cu at (116.3, 105.0)
- added T1: AO3400, MADW__SOT23, F.Cu at (114.0, 110.3)
- added U1: MCP1804-SOT23-5, MADW__SOT23-5, F.Cu at (116.3, 94.4)
- moved P1 53.6 mm to (90.8, 39.9)
- moved R2 53.6 mm to (94.0, 61.9)
- moved T1 53.6 mm to (90.8, 61.9)
- moved C1 53.6 mm to (87.3, 45.5)
- moved C2 53.6 mm to (93.3, 43.0)
- moved C3 53.6 mm to (89.8, 45.5)
- moved NJ1 53.6 mm to (89.8, 42.5)
- moved R1 53.6 mm to (87.6, 62.0)
- moved U1 53.6 mm to (93.2, 46.0)
- moved IC1 53.6 mm to (93.0, 50.9)
- moved JP1 53.6 mm to (88.5, 50.9)
- moved P2 53.6 mm to (90.8, 66.1)
- moved RV1 53.6 mm to (88.8, 56.6)
- moved RV2 53.6 mm to (93.1, 56.6)
- moved 1PIN 2.00 mm to (104.0, 84.0)
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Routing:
- net GNDPWR: track 246.5 -> 164.3 mm, vias 30 -> 20
- net /Vin: track 224.1 -> 149.4 mm, vias 6 -> 4
- net GND: track 204.8 -> 136.6 mm, vias 12 -> 8
- net /MOSI: track 175.1 -> 116.7 mm
- net VCC: track 119.8 -> 79.9 mm, vias 12 -> 8
- net /POT1: track 77.5 -> 51.6 mm
- net /SCK: track 70.7 -> 47.1 mm
- net /MISO: track 52.0 -> 34.6 mm
- net /POT2: track 51.1 -> 34.1 mm
- net /RESET: track 34.0 -> 22.7 mm
- net /drain: track 21.8 -> 14.5 mm
- net N-000004: track 16.5 -> 11.0 mm
